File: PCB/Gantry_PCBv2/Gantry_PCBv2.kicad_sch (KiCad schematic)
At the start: 160 parts, among them J1 Screw_Terminal_01x02, J10 B2B-XH-A_LF__SN_, J11 USB_C_Receptacle_USB2.0_16P, J12 Conn_01x04_Pin, J13 Conn_01x04_Pin, J14 Conn_01x04_Pin, J15 Conn_01x04_Pin, J16 Conn_01x05_Pin, J17 Conn_01x05_Pin, J2 DCJ200-10-A-XX-X_REVA, J3 Conn_01x03_Pin, J4 Conn_01x14, J5 B2B-XH-A_LF__SN_, J6 B2B-XH-A_LF__SN_, J7 B2B-XH-A_LF__SN_, J8 Conn_01x14, J9 Conn_01x10, Q1 NMOS, Q2 SS8050, Q3 SS8050, SW1 SW_0, SW2 SW_EN, SW3 SW_Push_DPDT, SW4 SW_Push_DPDT, SW5 SW_Push_DPDT, SW6 SW_Push_DPDT, U1 ESP32-WROOM-32E, U10 74HC245, U11 74HC245, U12 MCP23017_SO, U2 MP1584, U3 CH340C, U4 TLV75733PDBV, U5 DRV8825_STEPPER_MOTOR_DRIVER_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, U6 DRV8825_STEPPER_MOTOR_DRIVER_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, U7 TB6612FNG H-bridge Motor Driv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, U8 DRV8825_STEPPER_MOTOR_DRIVER_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, U9 DRV8825_STEPPER_MOTOR_DRIVER_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

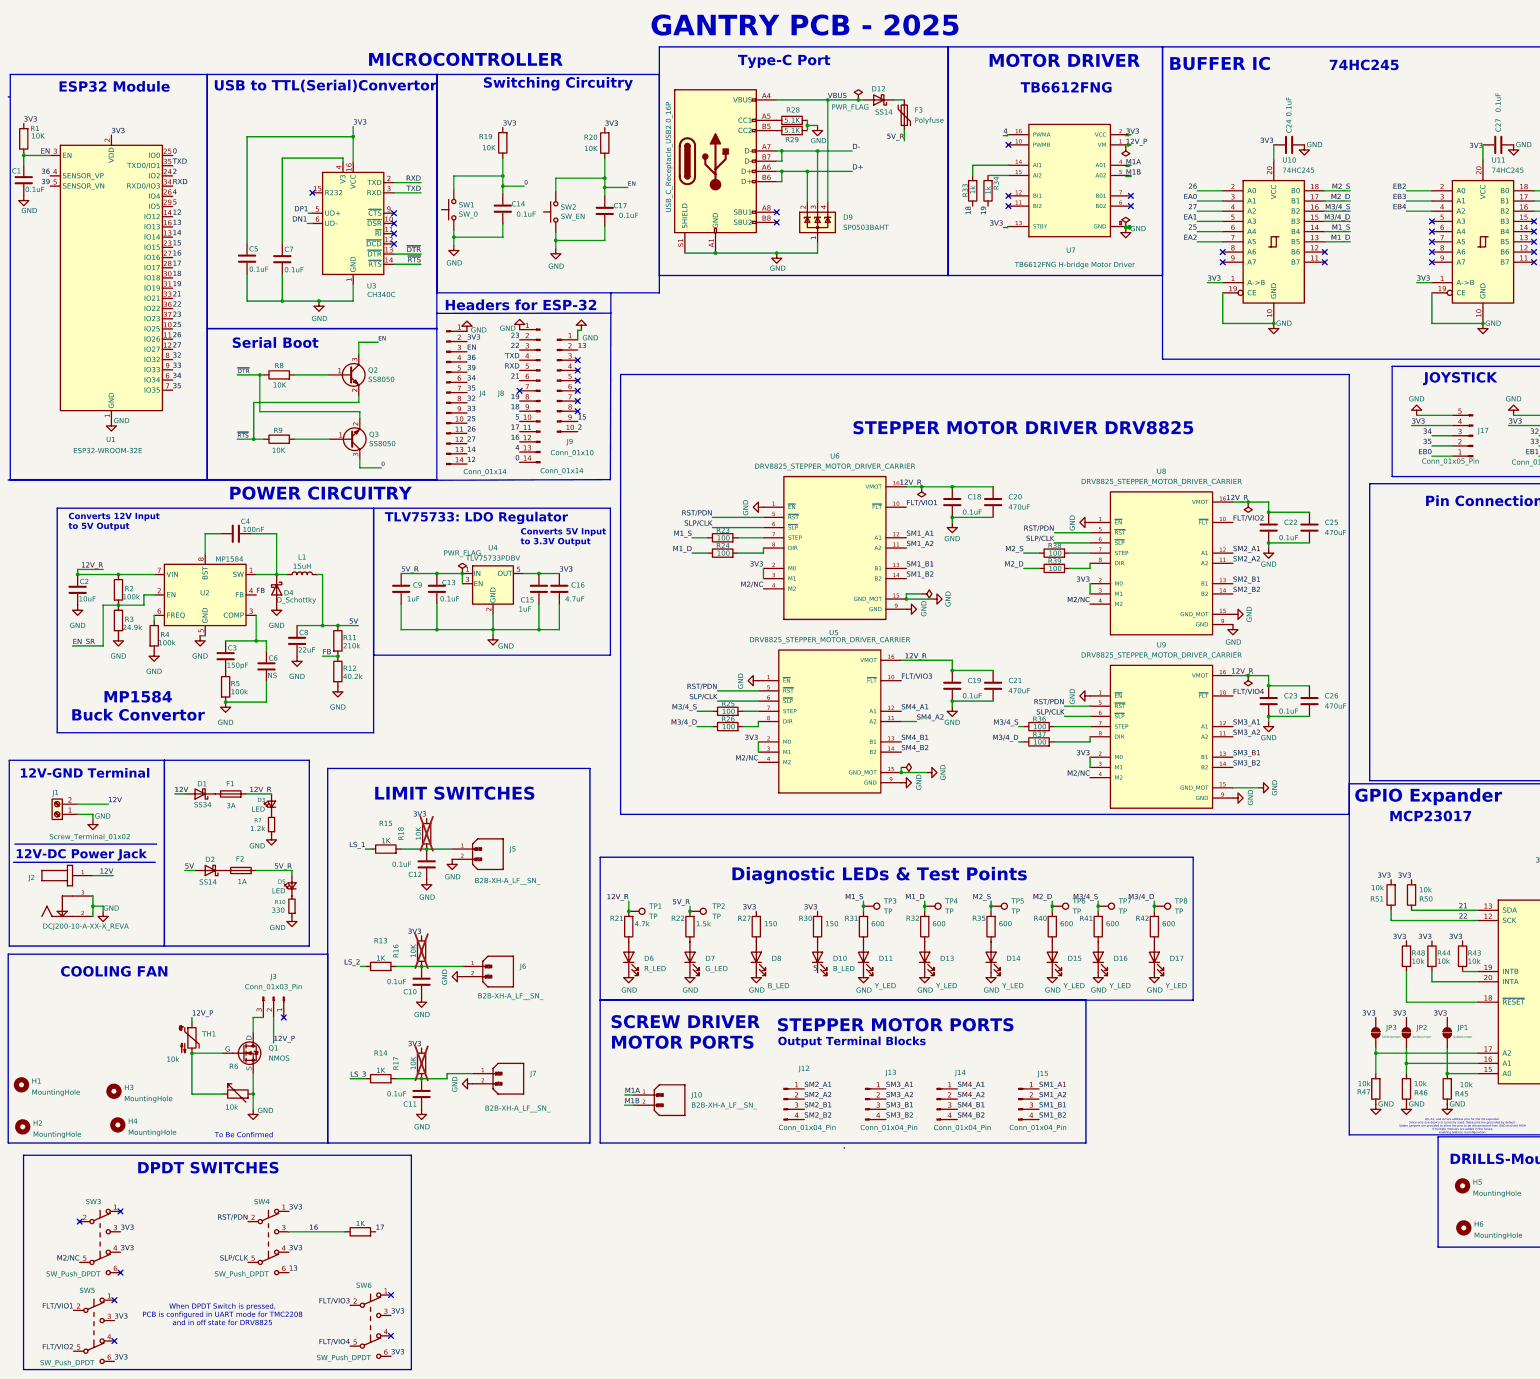
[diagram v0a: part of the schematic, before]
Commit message: Replaced CH340C with CP2102N and Wroom32U Symbol
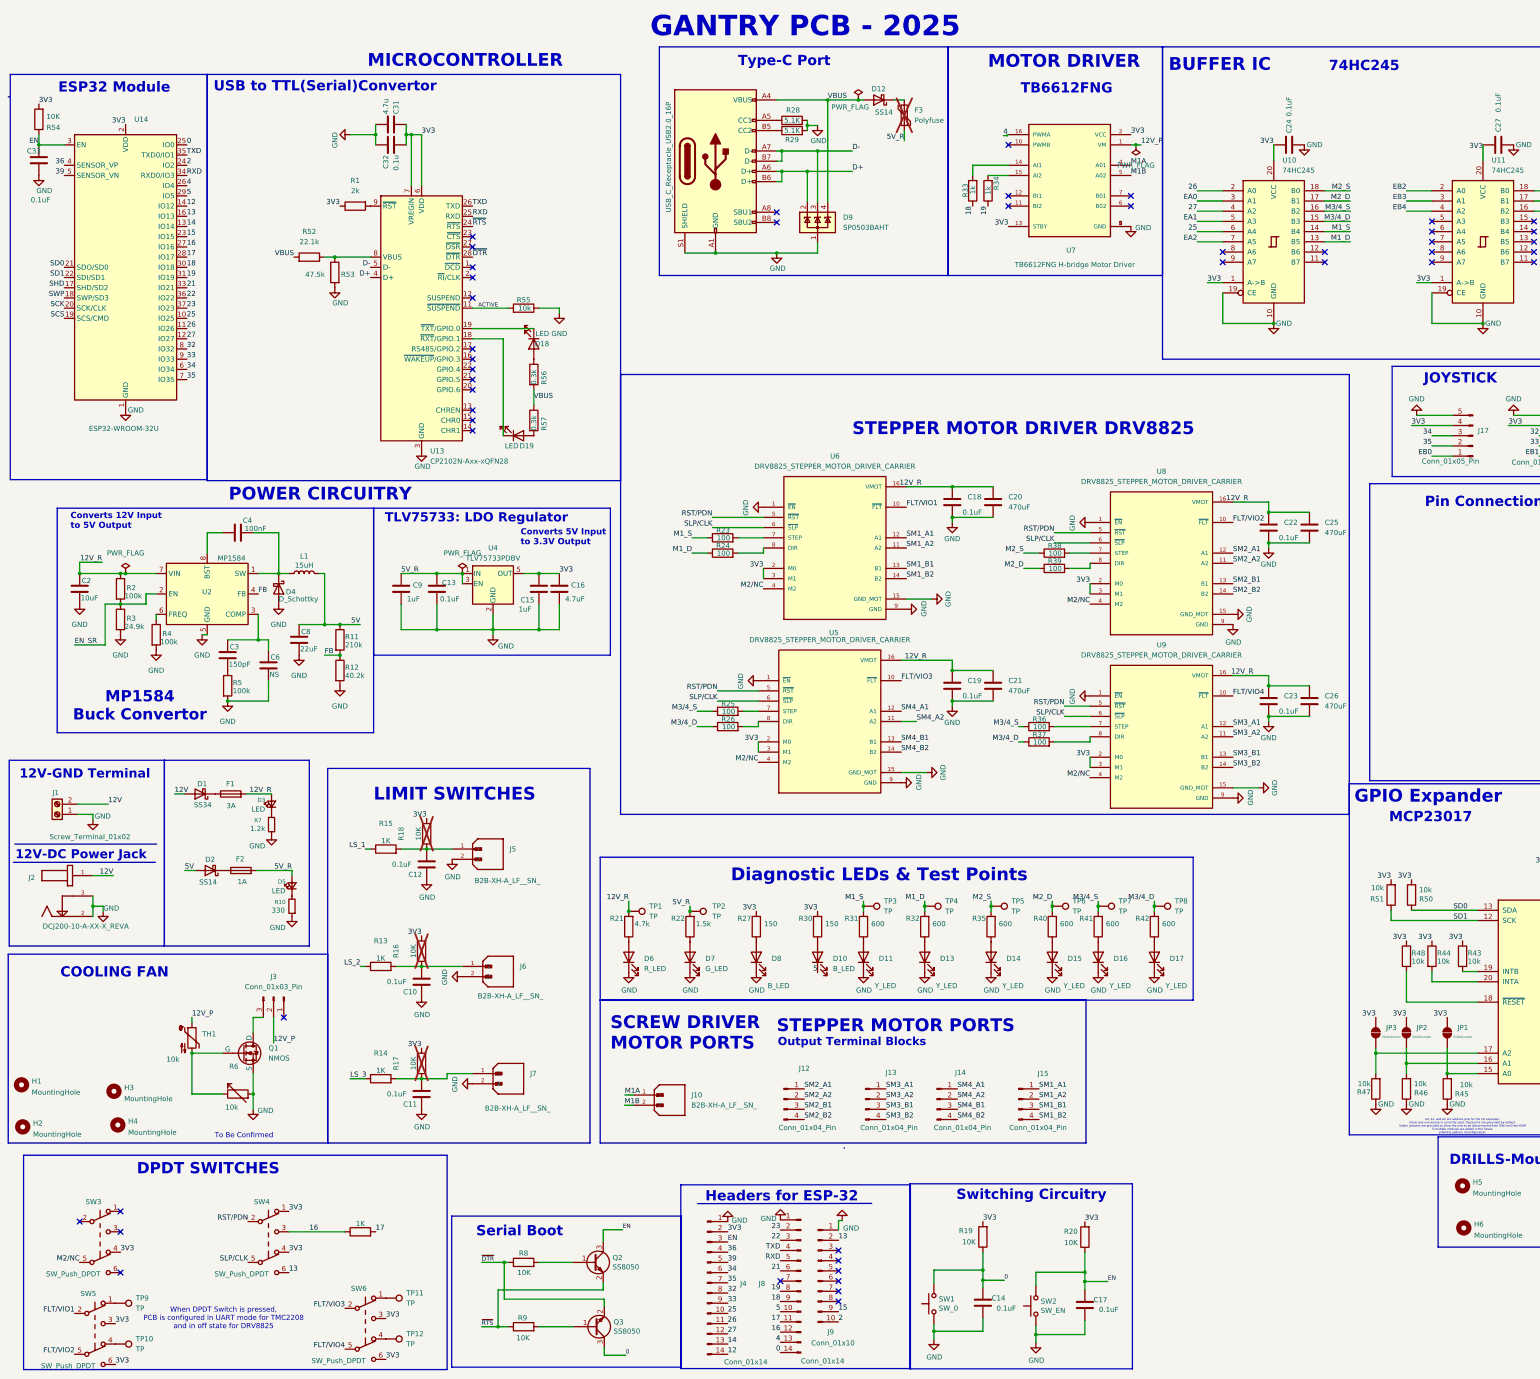
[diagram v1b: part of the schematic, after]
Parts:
- removed C1, C5, C7: 0.1uF, Capacitor_SMD:C_0805_2012Metric_Pad1.18x1.45mm_HandSolder, symbol ESP32-S2-rescue:C-Device
- removed R1: 10K, Resistor_SMD:R_0805_2012Metric_Pad1.20x1.40mm_HandSolder, symbol ESP32-S2-rescue:R-Device
- removed U1: ESP32-WROOM-32E, RF_Module:ESP32-WROOM-32E, symbol RF_Module:ESP32-WROOM-32E
- removed U3: CH340C, Package_SO:SOIC-16_3.9x9.9mm_P1.27mm, symbol ESP32-S2-rescue:CH340C-Interface_USB
- added C31: 4.7u, Capacitor_SMD:C_0805_2012Metric_Pad1.18x1.45mm_HandSolder, symbol Device:C
- added C32: 0.1u, Capacitor_SMD:C_0805_2012Metric_Pad1.18x1.45mm_HandSolder, symbol Device:C
- added C33: 0.1uF, Capacitor_SMD:C_0805_2012Metric_Pad1.18x1.45mm_HandSolder, symbol ESP32-S2-rescue:C-Device
- added D18, D19: LED, LED_SMD:LED_0805_2012Metric_Pad1.15x1.40mm_HandSolder, symbol Device:LED
- added R1: 2k, Resistor_SMD:R_0805_2012Metric_Pad1.20x1.40mm_HandSolder, symbol Device:R
- added R52: 22.1k, Resistor_SMD:R_0805_2012Metric_Pad1.20x1.40mm_HandSolder, symbol Device:R
- added R53: 47.5k, Resistor_SMD:R_0805_2012Metric_Pad1.20x1.40mm_HandSolder, symbol Device:R
- added R54: 10K, Resistor_SMD:R_0805_2012Metric_Pad1.20x1.40mm_HandSolder, symbol ESP32-S2-rescue:R-Device
- added R55: 10k, Resistor_SMD:R_0805_2012Metric_Pad1.20x1.40mm_HandSolder, symbol Device:R
- added R56, R57: 0.3k, Resistor_SMD:R_0805_2012Metric_Pad1.20x1.40mm_HandSolder, symbol Device:R
- added TP10, TP11, TP12, TP9: TP, TestPoint:TestPoint_Pad_D2.0mm, symbol Connector:TestPoint
- added U13: CP2102N-Axx-xQFN28, Package_DFN_QFN:QFN-28-1EP_5x5mm_P0.5mm_EP3.35x3.35mm, symbol Interface_USB:CP2102N-Axx-xQFN28
- added U14: ESP32-WROOM-32U, RF_Module:ESP32-WROOM-32U, symbol RF_Module:ESP32-WROOM-32U
- D10, D11, D13, D14, D15, D16, D17, D6, D7, D8: footprint LED_SMD:LED_0201_0603Metric_Pad0.64x0.40mm_HandSolder -> LED_SMD:LED_0805_2012Metric_Pad1.15x1.40mm_HandSolder
- D3, D5: footprint LED_SMD:LED_0603_1608Metric_Pad1.05x0.95mm_HandSolder -> LED_SMD:LED_0805_2012Metric_Pad1.15x1.40mm_HandSolder
- F3: DNP (none) -> Yes; now not fitted
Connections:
- net 0: now also U14.25 (IO0)
- net 12: now also U14.14 (IO12)
- net 13: now also U14.16 (IO13)
- net 14: now also U14.13 (IO14)
- net 15: now also U14.23 (IO15)
- net 16: now also U14.27 (IO16)
- net 17: now also U14.28 (IO17)
- net 18: now also U14.30 (IO18)
- net 19: now also U14.31 (IO19)
- net 2: now also U14.24 (IO2)
- net 21: now also U14.33 (IO21); no longer R50.1, U12.13 (SDA)
- net 22: now also U14.36 (IO22); no longer R51.1, U12.12 (SCK)
- net 23: now also U14.37 (IO23)
- net 25: now also U14.10 (IO25)
- net 26: now also U14.11 (IO26)
- net 27: now also U14.12 (IO27)
- net 32: now also U14.8 (IO32)
- net 33: now also U14.9 (IO33)
- net 34: now also U14.6 (IO34)
- net 35: now also U14.7 (IO35)
- net 36: now also U14.4 (SENSOR_VP)
- net 39: now also U14.5 (SENSOR_VN)
- net 3V3: now also C31.1, C32.2, R1.1, R54.2, U13.6 (VDD), U13.7 (VREGIN), U14.2 (VDD); no longer SW3.3 (C)
- net 4: now also U14.26 (IO4)
- net 5: now also U14.29 (IO5)
- net D+: now also U13.4 (D+)
- net D-: now also U13.5 (D-)
- net EN: now also C33.1, R54.1, U14.3 (EN)
- net GND: now also C31.2, C32.1, C33.2, R53.2, R55.1, U13.29 (GND), U13.3 (GND), U14.1 (GND), U14.15 (GND), U14.38 (GND), U14.39 (GND)
- net RXD: now also U13.25 (RXD), U14.34 (RXD0/IO3)
- net TXD: now also U13.26 (TXD), U14.35 (TXD0/IO1)
- net VBUS: now also R52.2, R56.2, R57.1
- net ~{DTR}: now also U13.28 (~{DTR})
- net ~{RTS}: now also U13.24 (~{RTS})
- net at SW6.1 (A): now also TP11.1
- net at SW6.4 (A): now also TP12.1
- net at SW5.1 (A): now also TP9.1
- net at SW5.4 (A): now also TP10.1
- new net: D18.1 (K), U13.19 (~{TXT}/GPIO.0)
- new net: D18.2 (A), R56.1
- new net: R52.1, R53.1, U13.8 (VBUS)
- new net: D19.1 (K), U13.18 (~{RXT}/GPIO.1)
- new net: D19.2 (A), R57.2
- new net: R1.2, U13.9 (~{RST})
- new net ACTIVE: R55.2, U13.11 (~{SUSPEND})
- new net SCK: U14.20 (SCK/CLK)
- new net SCS: U14.19 (SCS/CMD)
- new net SD0: R50.1, U12.13 (SDA), U14.21 (SDO/SD0)
- new net SD1: R51.1, U12.12 (SCK), U14.22 (SDI/SD1)
- new net SHD: U14.17 (SHD/SD2)
- new net SWP: U14.18 (SWP/SD3)
- no-connect marks 41 -> 46
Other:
- moved on the sheet: C14, C17, C2, C3, C4, C6, C8, D4, J4, J8, J9, L1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

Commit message: Minor Changes in Schematic, Initial Layout of PCB done
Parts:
- removed D3, D5: LED, LED_SMD:LED_0805_2012Metric_Pad1.15x1.40mm_HandSolder, symbol Device:LED_Small
- removed R10: 330, Resistor_SMD:R_0805_2012Metric_Pad1.20x1.40mm_HandSolder, symbol Device:R_Small
- removed R7: 1.2k, Resistor_SMD:R_0805_2012Metric_Pad1.20x1.40mm_HandSolder, symbol Device:R_Small
- added TP13: TP, TestPoint:TestPoint_Pad_D2.0mm, symbol Connector:TestPoint
- J10, J5, J6, J7: footprint 2 Pin JST_Power&Motors:JST_B2B-XH-A_LF__SN_ -> Connector_JST:JST_EH_B2B-EH-A_1x02_P2.50mm_Vertical
- J2: footprint Connector_BarrelJack:BarrelJack_Wuerth_6941xx301002 -> Connector_BarrelJack:BarrelJack_GCT_DCJ200-10-A_Horizontal
- SW3, SW4, SW5, SW6: footprint dpdt_tht:dpdt_sw_2x03_tht -> dpdt_tht:dpdt
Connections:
- net 3V3: now also TP13.1
- net SCK: now also J9.6 (Pin_6)
- net SCS: now also J9.5 (Pin_5)
- net SD0: now also J9.7 (Pin_7)
- net SD1: now also J9.8 (Pin_8)
- net SHD: now also J9.3 (Pin_3)
- net SWP: now also J9.4 (Pin_4)
- no-connect marks 46 -> 40
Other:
- moved on the sheet: D1, D2, D8, F1, F2, J9, R27

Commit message: Changed footprint of potentiometer
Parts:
- removed R6: 10k, Resistor_SMD:R_0805_2012Metric_Pad1.20x1.40mm_HandSolder, symbol Device:R_Variable
- added RV1: Potentiometer, Potentiometer_THT:Potentiometer_Bourns_3266Y_Vertical, symbol Device:R_Potentiometer
- F1: value 3A -> 5A
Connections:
- net 12V_P: now also RV1.3
- net at Q1.2 (G), TH1.2: now also RV1.1, RV1.2
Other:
- moved on the sheet: C10, C11, C12, C13, C14, C15, C16, C17, C18, C19, C2, C20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
